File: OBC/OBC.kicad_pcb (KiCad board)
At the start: 2 copper layers, 93 x 93 mm, 23 parts, among them J101 Modos de operación, J102 PMS-Raspi, J103 Conector UART, J104 Raspi-TRU, U101 RASPBERRY_PI_ZERO_2_W, U102 BMP280, U201 ADS1115IDGS

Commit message: Propone disposicion pcb
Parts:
- J103: footprint Connector_JST:JST_XH_S3B-XH-A-1_1x03_P2.50mm_Horizontal -> Connector_PinHeader_2.54mm:PinHeader_1x03_P2.54mm_Vertical
- moved R106 53.7 mm to (167.0, 57.5), turned to -90 degrees
- moved C202 52.5 mm to (174.8, 60.0), turned to 180 degrees
- moved R201 49.6 mm to (181.6, 61.9), turned to 0 degrees
- moved R105 47.6 mm to (172.0, 57.5), turned to -90 degrees
- moved R203 47.1 mm to (167.5, 64.8)
- moved R204 46.3 mm to (167.5, 61.6)
- moved C101 46.1 mm to (133.3, 58.8), turned to 180 degrees
- moved C201 43.9 mm to (174.7, 67.0), turned to 180 degrees
- moved R202 43.1 mm to (181.5, 64.5), turned to 0 degrees
- moved F101 43.0 mm to (133.9, 61.7), turned to 0 degrees
- moved R104 41.3 mm to (177.3, 57.4), turned to -90 degrees
- moved U201 41.1 mm to (174.7, 63.0), turned to 0 degrees
- moved R103 35.9 mm to (182.3, 57.4), turned to -90 degrees
- moved R101 23.2 mm to (127.7, 70.8)
- moved R102 23.2 mm to (127.7, 74.8)
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
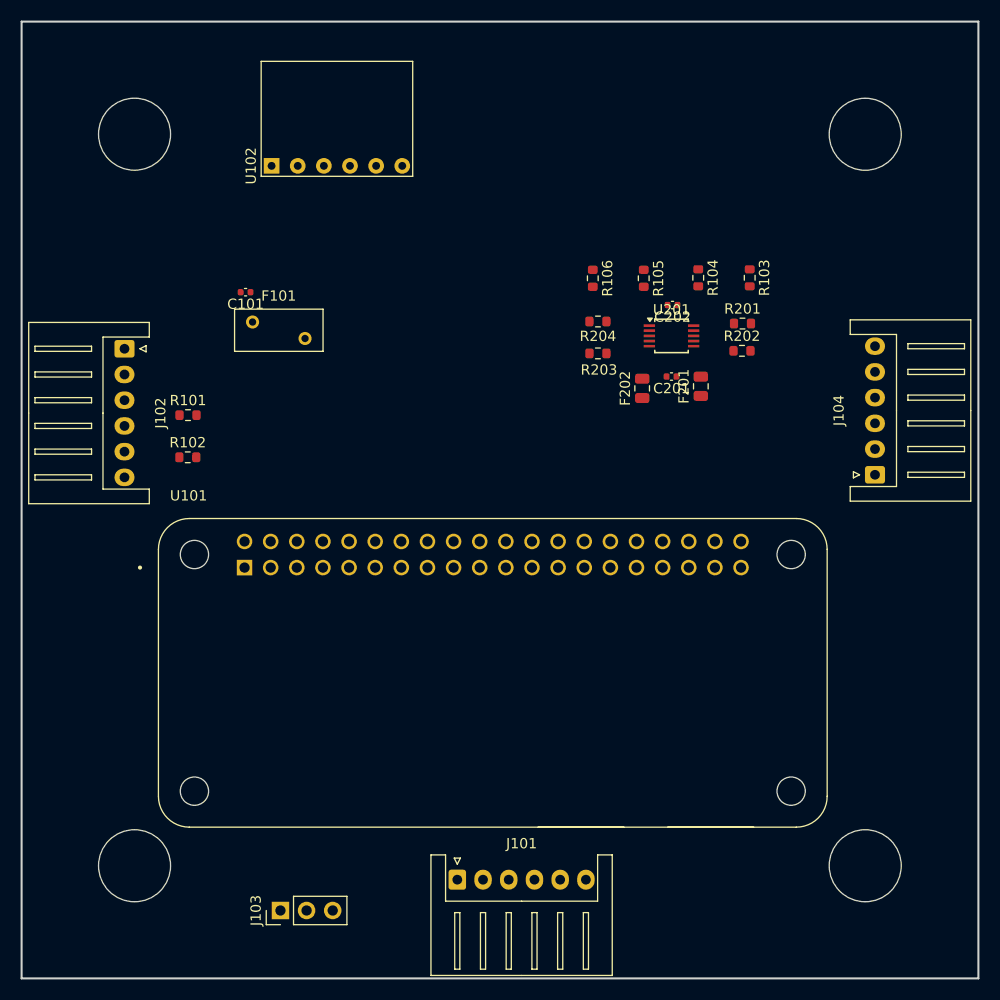
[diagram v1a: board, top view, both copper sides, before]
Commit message: Remueve hmi fisico del obs y renombra componentes
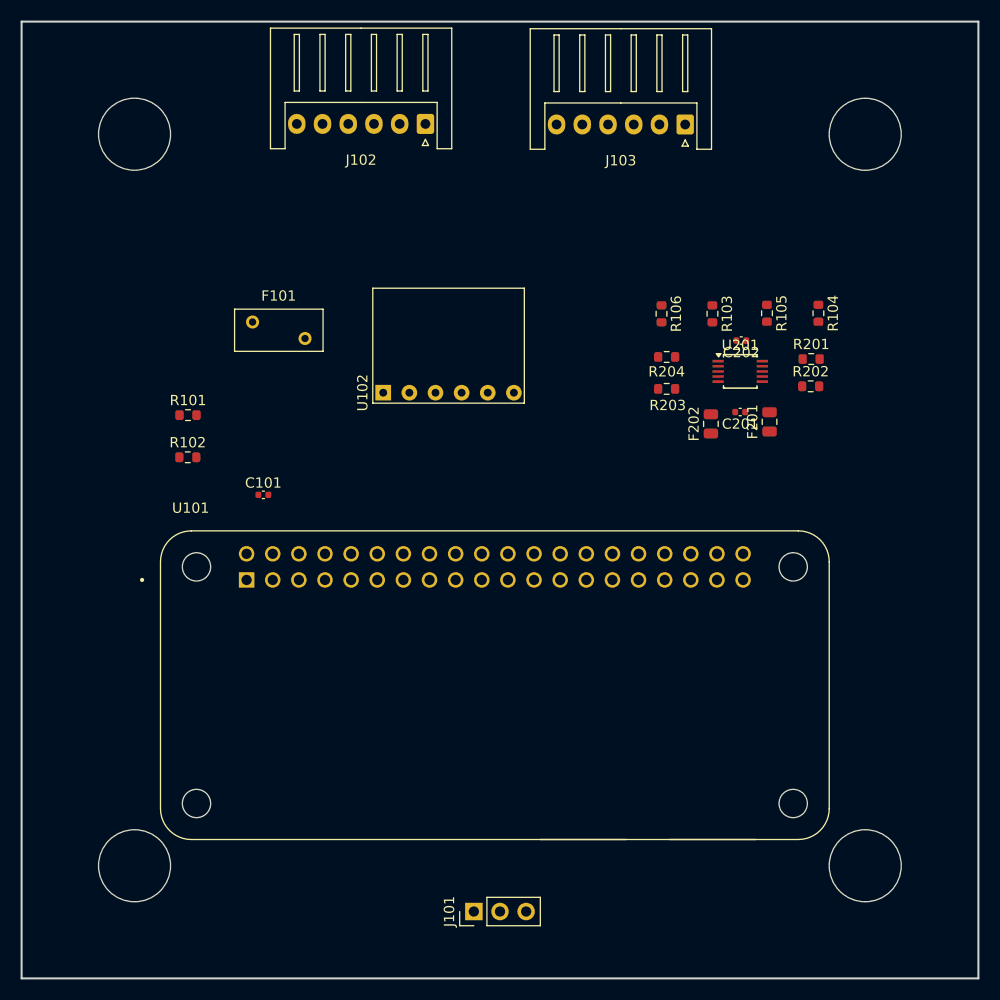
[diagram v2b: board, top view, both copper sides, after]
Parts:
- removed the J101 at (153.8, 115.9)
- R103: renamed from R105; value 10k -> R
- R104: renamed from R103; value 10k -> R
- R105: renamed from R104; value 10k -> R
- moved J103 38.7 mm to (176.0, 42.5), turned to 180 degrees
- moved J102 36.5 mm to (150.8, 42.4), turned to 180 degrees
- moved U102 24.6 mm to (146.7, 68.6)
- moved C101 19.8 mm to (135.0, 78.5), turned to 0 degrees
- moved J101 18.8 mm to (155.5, 119.0)
- moved C201 7.52 mm to (181.3, 70.5)
- moved U201 7.52 mm to (181.3, 66.5)
- moved R103 7.52 mm to (178.7, 60.9)
- moved R201 7.52 mm to (188.2, 65.3)
- moved F202 7.52 mm to (178.5, 71.6)
- moved C202 7.52 mm to (181.4, 63.5)
- moved F201 7.52 mm to (184.2, 71.4)
- moved R104 7.52 mm to (188.9, 60.9)
- moved R105 7.52 mm to (183.9, 60.9)
- moved R202 7.52 mm to (188.2, 68.0)
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- renumbered J103 to J101, J104 to J103
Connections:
- J103 pad 4: /AIN3 -> unconnected-(J103-Pin_4-Pad4)
- J103 pad 5: +5V PMS -> unconnected-(J103-Pin_5-Pad5)
- J103 pad 6: GND -> +5V PMS
- U101 pad 11: /~{MODE_SEL0} -> unconnected-(U101-GPIO17/GPIO_GEN0-Pad11)
- U101 pad 13: /~{MODE_SEL2} -> unconnected-(U101-GPIO27/GPIO_GEN2-Pad13)
- U101 pad 14: unconnected-(U101-GND_14-Pad14) -> GND
- U101 pad 15: /~{MODE_SEL1} -> unconnected-(U101-GPIO22/GPIO_GEN3-Pad15)
- U101 pad 20: unconnected-(U101-GND_20-Pad20) -> GND
- U101 pad 25: unconnected-(U101-GND_25-Pad25) -> GND
- U101 pad 30: unconnected-(U101-GND_30-Pad30) -> GND
- U101 pad 34: unconnected-(U101-GND_34-Pad34) -> GND
- U101 pad 39: unconnected-(U101-GND_39-Pad39) -> GND
- U101 pad 4: unconnected-(U101-5V_4-Pad4) -> Net-(U101-5V_2)
- U101 pad 9: unconnected-(U101-GND_9-Pad9) -> GND
- U201 pad 7: /AIN3 -> /ADS1115_ADC/AIN3
